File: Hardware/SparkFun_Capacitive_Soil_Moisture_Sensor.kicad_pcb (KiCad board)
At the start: 2 copper layers, 15.2 x 76.2 mm, 57 parts, among them J1 Qwiic_RA, J2 Qwiic_RA, U1 CY8CMBR3102

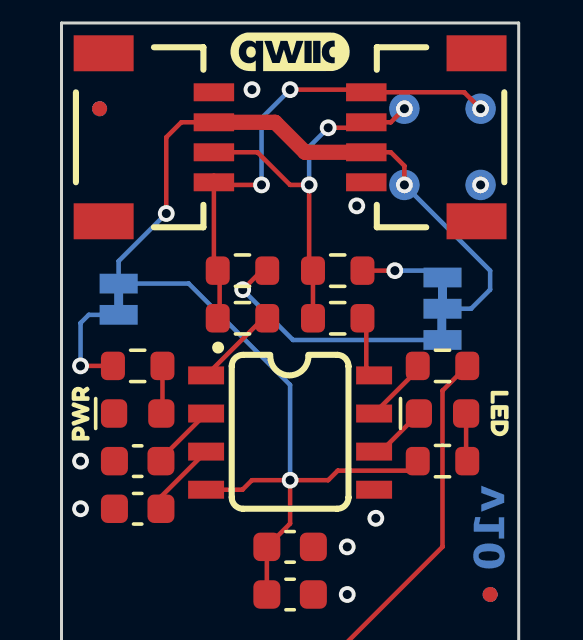
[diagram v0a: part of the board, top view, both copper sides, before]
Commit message: Remove the 330 ohm series I2C resistors.
These resistors cause issues when you daisy chain qwiic devices as they
form a voltage divider with the pull-up resistance.
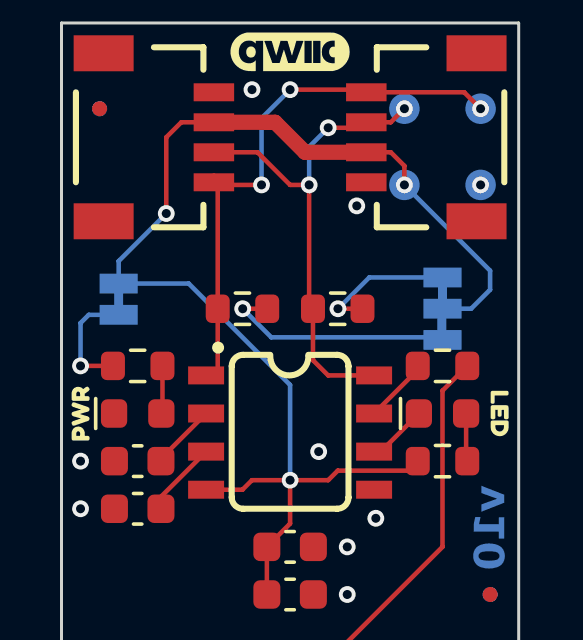
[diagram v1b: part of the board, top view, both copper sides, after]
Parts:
- removed R4, R5: 330, SparkFun-Resistor:R_0603_1608Metric
- moved R2 1.27 mm to (114.0, 57.8)
- moved R3 1.27 mm to (117.2, 57.8)
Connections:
- U1 pad 1: Net-(U1-SCL) -> SCL
- U1 pad 8: Net-(U1-SDA) -> SDA
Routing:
- net SDA: track 13.2 -> 16.7 mm
- net Net-(U1-SCL): track 2.89 -> 0.00 mm
- net SCL: track 16.5 -> 19.1 mm
- net Net-(U1-SDA): track 2.07 -> 0.00 mm
- net Net-(JP2-A): track 2.83 -> 4.73 mm
- net Net-(JP2-C): track 8.63 -> 7.91 mm
- net GND: vias 8 -> 9

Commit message: Add changes from final review
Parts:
- moved C1 2.25 mm to (114.0, 65.7)
- moved C2 1.59 mm to (117.2, 65.7)
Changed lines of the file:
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@@
 	(title_block
 		(title "SparkFun Capacitive Soil Moisture Sensor (Qwiic)")
-		(date "2025-12-11")
+		(date "2026-02-04")
 		(rev "v10")
 		(company "SparkFun")
@@
 	(footprint "SparkFun-Capacitor:C_0603_1608Metric"
 		(layer "F.Cu")
-		(at 115.57 65.7225)
+		(at 117.1575 65.7225)
 		(tags "SparkFun capacitor")
 		(property "Reference" "C2"
@@
 	(footprint "SparkFun-Capacitor:C_0603_1608Metric"
 		(layer "F.Cu")
-		(at 115.57 67.31)
+		(at 113.9825 65.7225)
 		(tags "SparkFun capacitor")
 		(property "Reference" "C1"
@@
 			(keep_text_aligned yes)
 		)
-		(gr_text "0.6 in"
+		(gr_text "600 mils"
 			(at 105.156 44.196 0)
 			(layer "Dwgs.User")
@@
 			(keep_text_aligned yes)
 		)
-		(gr_text "0.88 in"
+		(gr_text "880 mils"
 			(at 129.794 44.7915 90)
 			(layer "Dwgs.User")
@@
 			(keep_text_aligned yes)
 		)
-		(gr_text "0.5 in"
+		(gr_text "500 mils"
 			(at 127.762 45.2995 90)
 			(layer "Dwgs.User")
@@
 			(keep_text_aligned yes)
 		)
-		(gr_text "0.1 in"
+		(gr_text "100 mils"
 			(at 105.156 45.974 0)
 			(layer "Dwgs.User")
@@
 			(keep_text_aligned yes)
 		)
-		(gr_text "3 in"
+		(gr_text "3000 mils"
 			(at 133.858 45.72 90)
 			(layer "Dwgs.User")
@@
 			(keep_text_aligned yes)
 		)
-		(gr_text "1 in"
+		(gr_text "1000 mils"
 			(at 131.826 45.72 90)
 			(layer "Dwgs.User")
@@
 			(keep_text_aligned yes)
 		)
-		(gr_text "0.15 in"
+		(gr_text "150 mils"
 			(at 125.73 44.704 90)
 			(layer "Dwgs.User")
@@
 	)
 	(segment
-		(start 114.935 67.31)
-		(end 114.795 67.31)
+		(start 116.84 63.5)
+		(end 115.57 63.5)
 		(width 0.1524)
 		(layer "F.Cu")
@@
 	)
 	(segment
-		(start 116.84 63.5)
-		(end 115.57 63.5)
+		(start 115.57 63.5)
+		(end 115.57 64.135)
 		(width 0.1524)
 		(layer "F.Cu")
@@
 	)
 	(segment
-		(start 114.795 65.7225)
-		(end 115.57 64.9475)
-		(width 0.1524)
-		(layer "F.Cu")
-		(net 1)
-	)
-	(segment
 		(start 115.57 63.5)
 		(end 114.3 63.5)
@@
 	)
 	(segment
-		(start 115.57 64.9475)
-		(end 115.57 63.5)
+		(start 119.825 62.865)
+		(end 119.5075 63.1825)
 		(width 0.1524)
 		(layer "F.Cu")
@@
 	)
 	(segment
-		(start 119.825 62.865)
-		(end 119.5075 63.1825)
+		(start 117.1575 63.1825)
+		(end 116.84 63.5)
 		(width 0.1524)
 		(layer "F.Cu")
@@
 	)
 	(segment
-		(start 117.1575 63.1825)
-		(end 116.84 63.5)
+		(start 113.2075 64.9475)
+		(end 113.2075 65.7225)
 		(width 0.1524)
 		(layer "F.Cu")
@@
 	)
 	(segment
+		(start 115.57 64.135)
+		(end 116.3825 64.9475)
+		(width 0.1524)
+		(layer "F.Cu")
+		(net 1)
+	)
+	(segment
 		(start 111.4425 52.07)
 		(end 111.9425 51.57)
@@
 	)
 	(segment
-		(start 113.03 51.57)
-		(end 114.808 51.57)
-		(width 0.508)
+		(start 112.77 64.51)
+		(end 113.2075 64.9475)
+		(width 0.1524)
 		(layer "F.Cu")
 		(net 1)
 	)
 	(segment
-		(start 114.795 67.31)
-		(end 114.795 65.7225)
-		(width 0.1524)
+		(start 113.03 51.57)
+		(end 114.808 51.57)
+		(width 0.508)
 		(layer "F.Cu")
 		(net 1)
@@
 	)
 	(segment
+		(start 116.3825 64.9475)
+		(end 116.3825 65.7225)
+		(width 0.1524)
+		(layer "F.Cu")
+		(net 1)
+	)
+	(segment
 		(start 113.9825 63.8175)
 		(end 112.9605 63.8175)
@@
 	)
 	(segment
+		(start 112.77 63.8175)
+		(end 112.77 64.51)
+		(width 0.1524)
+		(layer "F.Cu")
+		(net 1)
+	)
+	(segment
 		(start 119.38 53.0225)
 		(end 118.9275 52.57)
@@
 	)
 	(via
-		(at 117.475 65.7225)
+		(at 119.0625 65.7225)
 		(size 0.56)
 		(drill 0.3)
@@
 	)
 	(via
-		(at 117.475 67.31)
+		(at 114.935 66.675)
 		(size 0.56)
 		(drill 0.3)
@@
 	)
 	(segment
+		(start 108.669217 59.69)
+		(end 108.666039 59.693178)
+		(width 0.1524)
+		(layer "F.Cu")
+		(net 6)
+	)
+	(segment
 		(start 109.665 59.69)
-		(end 108.585 59.69)
+		(end 108.669217 59.69)
 		(width 0.1524)
 		(layer "F.Cu")
@@
 	)
 	(via
-		(at 108.585 59.69)
+		(at 108.666039 59.693178)
 		(size 0.56)
 		(drill 0.3)
@@
 	)
 	(segment
-		(start 108.85805 57.9882)
-		(end 108.585 58.26125)
+		(start 108.585 58.26125)
+		(end 108.85805 57.9882)
 		(width 0.1524)
 		(layer "B.Cu")
@@
 	)
 	(segment
-		(start 108.585 58.26125)
-		(end 108.585 59.69)
+		(start 108.666039 59.693178)
+		(end 108.585 59.612139)
 		(width 0.1524)
 		(layer "B.Cu")
@@
 	)
 	(segment
-		(start 109.855 57.9882)
-		(end 108.85805 57.9882)
+		(start 108.85805 57.9882)
+		(end 109.855 57.9882)
+		(width 0.1524)
+		(layer "B.Cu")
+		(net 6)
+	)
+	(segment
+		(start 108.585 59.612139)
+		(end 108.585 58.26125)
 		(width 0.1524)
 		(layer "B.Cu")

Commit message: Add metric ruler
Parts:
- removed kibuzzard-69693786: G***, kibuzzard-69693786
- removed kibuzzard-696937B5: G***, kibuzzard-696937B5
- removed kibuzzard-696937B9: G***, kibuzzard-696937B9
- removed kibuzzard-696937BE: G***, kibuzzard-696937BE
- removed kibuzzard-696937C3: G***, kibuzzard-696937C3
- removed kibuzzard-696937C9: G***, kibuzzard-696937C9
- removed kibuzzard-696937DE: G***, kibuzzard-696937DE
- added kibuzzard-6983799B: G***, kibuzzard-6983799B, B.Cu at (114.6, 76.0)
- added kibuzzard-69837BBB: G***, kibuzzard-69837BBB, B.Cu at (116.6, 114.3)
- added kibuzzard-69837BD1: G***, kibuzzard-69837BD1, B.Cu at (116.6, 109.3)
- added kibuzzard-69837BDA: G***, kibuzzard-69837BDA, B.Cu at (116.6, 104.3)
- added kibuzzard-69837BE0: G***, kibuzzard-69837BE0, B.Cu at (116.6, 99.3)
- added kibuzzard-69837BE5: G***, kibuzzard-69837BE5, B.Cu at (116.6, 94.3)
- added kibuzzard-69837BE9: G***, kibuzzard-69837BE9, B.Cu at (116.6, 89.3)
- added kibuzzard-69837BEE: G***, kibuzzard-69837BEE, B.Cu at (116.6, 84.3)
- added kibuzzard-69837BF5: G***, kibuzzard-69837BF5, B.Cu at (116.6, 79.3)

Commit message: Center max line
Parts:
- moved kibuzzard-6983799B 1.08 mm to (115.6, 75.6)
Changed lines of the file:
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@@
 	(footprint "kibuzzard-6983799B"
 		(layer "B.Cu")
-		(at 114.584 76 180)
+		(at 115.57 75.565 180)
 		(descr "Generated with KiBuzzard")
 		(tags "kb_params=eyJBbGlnbm1lbnRDaG9pY2UiOiAiQ2VudGVyIiwgIkNhcExlZnRDaG9pY2UiOiAiKCIsICJDYXBSaWdodENob2ljZSI6ICJdIiwgIkZvbnRDb21ib0JveCI6ICJGcmVkZHlTcGFyay1SZWd1bGFyIiwgIkhlaWdodEN0cmwiOiAxLjQsICJMYXllckNvbWJvQm94IjogIkYuU2lsa1MiLCAiTGluZVNwYWNpbmdDdHJsIjogMS41LCAiTXVsdGlMaW5lVGV4dCI6ICJNYXggICg1MG1tKSIsICJQYWRkaW5nQm90dG9tQ3RybCI6IDMuMCwgIlBhZGRpbmdMZWZ0Q3RybCI6IDMuMCwgIlBhZGRpbmdSaWdodEN0cmwiOiAzLjAsICJQYWRkaW5nVG9wQ3RybCI6IDMuMCwgIldpZHRoQ3RybCI6IDEuMywgImFkdmFuY2VkQ2hlY2tib3giOiB0cnVlLCAiaW5saW5lRm9ybWF0VGV4dGJveCI6IHRydWUsICJsaW5lb3ZlclN0eWxlQ2hvaWNlIjogIlNxdWFyZSIsICJsaW5lb3ZlclRoaWNrbmVzc0N0cmwiOiAxfQ==")
